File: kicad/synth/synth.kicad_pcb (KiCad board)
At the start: 2 copper layers, 21 parts, among them J1 Barrel_Jack, J2 Conn_02x04_Top_Bottom, J3 Conn_02x04_Top_Bottom, J4 Conn_02x04_Top_Bottom, J5 Conn_02x04_Top_Bottom, J6 Conn_01x03_Socket

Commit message: fix button behaviour now I have a PCB
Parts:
- removed PICO1: PICO_L, Connector_PinSocket_2.54mm:PinSocket_1x20_P2.54mm_Vertical
- removed PICO2: PICO_R, Connector_PinSocket_2.54mm:PinSocket_1x20_P2.54mm_Vertical
- removed PWR_LED1, RESET_BTN1: Power IN, Connector_PinHeader_2.54mm:PinHeader_1x02_P2.54mm_Vertical
- removed R7: R, Resistor_SMD:R_0805_2012Metric_Pad1.20x1.40mm_HandSolder
- added J7: RESET_BTN_HEADER, Connector_PinHeader_1.00mm:PinHeader_1x02_P1.00mm_Vertical, F.Cu at (129.9, 110.6)
- added J8: POWER_IN, Connector_PinHeader_1.00mm:PinHeader_1x02_P1.00mm_Vertical, F.Cu at (133.3, 110.6)
- added J9: USB_A, Connector_USB:USB_A_CNCTech_1001-011-01101_Horizontal, F.Cu at (126.7, 147.4)
- added U1: Pico, MCU_RaspberryPi_and_Boards:RPi_Pico_SMD_TH, F.Cu at (97.9, 93.7)
- J1: value Barrel_Jack -> PWR_LED_HEADER; footprint Capacitor_SMD:C_0805_2012Metric_Pad1.18x1.45mm_HandSolder -> Connector_PinHeader_1.00mm:PinHeader_1x02_P1.00mm_Vertical
- J6: value Conn_01x03_Socket -> AUDIO_OUT
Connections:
- J1 pad 1: +5V -> GND
- J1 pad 2: GND -> /PWR_LED
- J2 pad 2: +5V -> GND
- J2 pad 4: /CS1 -> /CLK
- J2 pad 5: /CLK -> /CS1
- J2 pad 7: /SI -> /CS0
- J2 pad 8: /CS0 -> /SI
- J3 pad 2: +5V -> GND
- J3 pad 4: /CS5 -> /CLK
- J3 pad 5: /CLK -> /CS5
- J3 pad 7: /SI -> /CS4
- J3 pad 8: /CS4 -> /SI
- J4 pad 2: +5V -> GND
- J4 pad 4: /CS3 -> /CLK
- J4 pad 5: /CLK -> /CS3
- J4 pad 7: /SI -> /CS2
- J4 pad 8: /CS2 -> /SI
- J5 pad 2: +5V -> GND
- J5 pad 4: /CS7 -> /CLK
- J5 pad 5: /CLK -> /CS7
- J5 pad 7: /SI -> /CS6
- J5 pad 8: /CS6 -> /SI

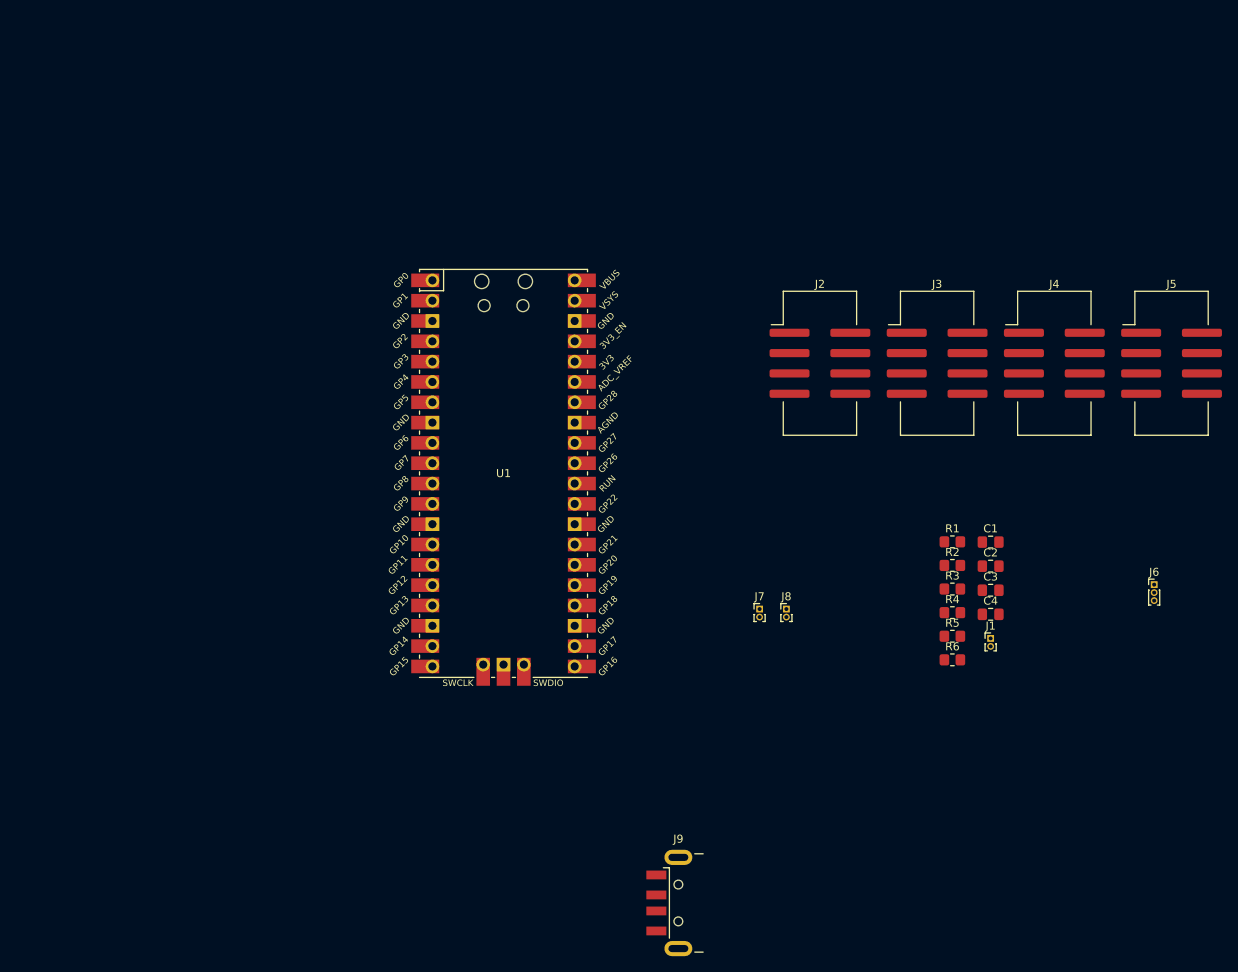
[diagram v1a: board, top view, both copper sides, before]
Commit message: USB PIO now works and can control via PC or direct MIDI device :)
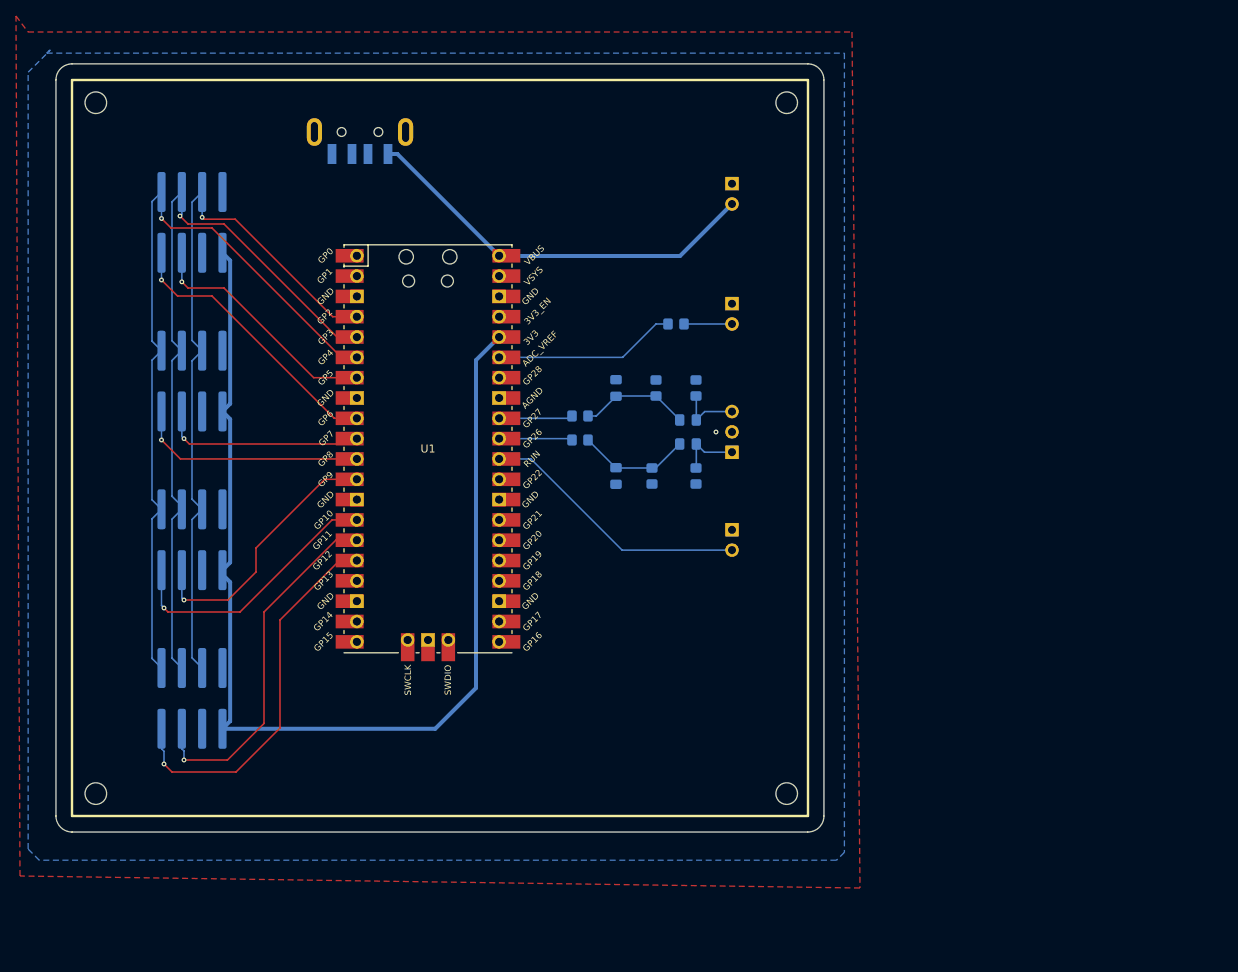
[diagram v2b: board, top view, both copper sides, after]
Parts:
- added H1: MountingHole, MountingHole:MountingHole_2.7mm_M2.5, F.Cu at (47.0, 47.3)
- added H2: MountingHole, MountingHole:MountingHole_2.7mm_M2.5, F.Cu at (47.0, 133.7)
- added H3: MountingHole, MountingHole:MountingHole_2.7mm_M2.5, F.Cu at (133.3, 133.7)
- added H4: MountingHole, MountingHole:MountingHole_2.7mm_M2.5, F.Cu at (133.3, 47.3)
- added R7: 1K, Resistor_SMD:R_0805_2012Metric_Pad1.20x1.40mm_HandSolder, B.Cu at (119.5, 75.0)
- C1, C2, C3, C4, J2, J3, J4, J5, J9, R1, R2, R3, R4, R5, R6: moved to B.Cu
- J1, J7, J8: footprint Connector_PinHeader_1.00mm:PinHeader_1x02_P1.00mm_Vertical -> Connector_PinHeader_2.54mm:PinHeader_1x02_P2.54mm_Vertical; moved to B.Cu
- J6: footprint Connector_PinHeader_1.00mm:PinHeader_1x03_P1.00mm_Vertical -> Connector_PinHeader_2.54mm:PinHeader_1x03_P2.54mm_Vertical; moved to B.Cu
- moved J5 129.4 mm to (59.0, 121.8), turned to 90 degrees
- moved J9 113.3 mm to (80.0, 44.1), turned to 90 degrees
- moved J4 107.8 mm to (59.0, 82.1), turned to 90 degrees
- moved J3 95.7 mm to (59.0, 102.0), turned to 90 degrees
- moved J2 80.4 mm to (59.0, 62.3), turned to 90 degrees
- moved J6 55.3 mm to (126.5, 91.0)
- moved J8 53.6 mm to (126.5, 57.5), turned to 180 degrees
- moved J1 52.9 mm to (126.5, 72.5), turned to 180 degrees
- moved C2 51.9 mm to (112.0, 83.0), turned to 90 degrees
- moved R2 50.2 mm to (107.5, 86.5)
- moved R1 48.3 mm to (107.5, 89.5)
- moved C1 47.6 mm to (112.0, 94.0), turned to 90 degrees
- moved R4 46.5 mm to (117.0, 83.0), turned to 90 degrees
- moved C4 45.0 mm to (121.0, 87.0)
- moved R5 44.6 mm to (122.0, 83.0), turned to -90 degrees
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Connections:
- C3 pad 2: unconnected-(C3-Pad2) -> /AUD_L
- J1 pad 2: /PWR_LED -> Net-(J1-Pin_2)
- U1 pad 10: /CS2 -> /CS3
- U1 pad 11: /CS3 -> /CS2
- U1 pad 12: /CS4 -> /CS5
- U1 pad 14: /CS5 -> /CS4
- U1 pad 15: /CS6 -> /CS7
- U1 pad 16: /CS7 -> /CS6
- U1 pad 7: /CS0 -> /CS1
- U1 pad 9: /CS1 -> /CS0
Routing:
- net +3V3: track 0.00 -> 140.8 mm
- net /SI: track 0.00 -> 95.4 mm, vias 0 -> 1
- net /SO: track 0.00 -> 94.0 mm, vias 0 -> 1
- net /CLK: track 0.00 -> 90.3 mm, vias 0 -> 1
- net +5V: track 0.00 -> 51.0 mm
- net /CS6: track 0.00 -> 48.6 mm, vias 0 -> 1
- net /CS7: track 0.00 -> 45.2 mm, vias 0 -> 1
- net /CS0: track 0.00 -> 36.5 mm, vias 0 -> 1
- net /CS4: track 0.00 -> 33.9 mm, vias 0 -> 1
- net /RESET: track 0.00 -> 33.8 mm
- net /CS5: track 0.00 -> 33.5 mm, vias 0 -> 1
- net /CS1: track 0.00 -> 30.5 mm, vias 0 -> 1
- net /CS2: track 0.00 -> 29.0 mm, vias 0 -> 1
- net /CS3: track 0.00 -> 25.7 mm, vias 0 -> 1
- net /PWR_LED: track 0.00 -> 23.1 mm
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- added copper zone on B.Cu, net GND
- added copper zone on F.Cu, net GND
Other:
- board outline added: 96 x 96 mm
- board text added: "TOP"
